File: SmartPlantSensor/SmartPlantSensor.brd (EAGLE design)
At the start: 25 x 100 mm, 13 parts

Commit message: Release v1.0.0
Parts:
- removed C5: 10nF, rcl:C0603
- removed U$1: TLC555CDR, HeRo:SOIC127P600X175-8
- removed U$2: ESP-12E, HeRo:ESP-12E
- added C1: 10nF, rcl:C0603
- added DS18B20: DS18B20Z+, MaximIntegrated:SOIC8
- added ESP-12E: ESP-12E, ESP:ESP-12E
- added JP10, JP11, JP12, JP13, JP14, JP3, JP4, JP5, JP6, JP7, JP8, JP9: (no value), pinhead:1X01
- added R10, R11, R7, R8, R9: 10k, rcl:R0603
- added TLC555: TLC555CD, TexasInstruments:SOIC8
- moved R6 1.53 mm to (7.24, 85.0), turned to 90 degrees
- moved R4 0.65 mm to (15.9, 92.8)
- moved C4 0.65 mm to (12.8, 92.8)
- moved R1 0.65 mm to (9.78, 85.5)
- moved C3 0.65 mm to (18.4, 88.3)
- moved R5 0.65 mm to (18.4, 91.3)
- moved C2 0.65 mm to (9.78, 89.5)
- moved R2 0.65 mm to (9.78, 87.5)
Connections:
- removed net N$7: C5.2, U$1.5
- new net 1WIRE: DS18B20.4, ESP-12E.19
- new net EN: ESP-12E.3, R7.1
- new net IO0: ESP-12E.18, JP6.1, R9.1
- new net IO12: ESP-12E.6, JP12.1
- new net IO13: ESP-12E.7, JP11.1
- new net IO14: ESP-12E.5, JP13.1
- new net IO15: ESP-12E.16, R8.2
- new net IO16: ESP-12E.4, JP14.1
- new net IO2: ESP-12E.17, R11.1
- new net N$1: C1.2, TLC555.5
- new net RST: ESP-12E.1, JP5.1, R10.1
- new net RXD: ESP-12E.21, JP8.1
- new net TXD: ESP-12E.22, JP7.1
- net +3V3: now also DS18B20.3, ESP-12E.8, JP3.1, JP9.1, R10.2, R11.2, R7.2, R9.2, TLC555.4, TLC555.8; no longer U$1.4, U$1.8, U$2.VCC
- net ADC: now also ESP-12E.2; no longer U$2.ADC
- net DISH: now also TLC555.7; no longer U$1.7
- net GND: now also C1.1, DS18B20.5, ESP-12E.15, JP10.1, JP4.1, R8.1, TLC555.1; no longer C5.1, U$1.1, U$2.GND
- net OUT: now also TLC555.3; no longer U$1.3
- net T: now also TLC555.2, TLC555.6; no longer U$1.2, U$1.6
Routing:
- net GND: track 1.63 -> 159.1 mm, vias 1 -> 3
- net SENSOR: track 10.0 -> 73.8 mm
- net RST: track 0.00 -> 28.4 mm, vias 0 -> 2
- net IO0: track 0.00 -> 15.8 mm, vias 0 -> 1
- net IO2: track 0.00 -> 11.6 mm, vias 0 -> 1
- net RXD: track 0.00 -> 10.8 mm, vias 0 -> 1
- net +3V3: track 7.56 -> 17.6 mm, vias 2 -> 4
- net TXD: track 0.00 -> 9.01 mm
- net 1WIRE: track 0.00 -> 7.14 mm, vias 0 -> 1
- net EN: track 0.00 -> 6.81 mm, vias 0 -> 1
- net IO15: track 0.00 -> 5.46 mm, vias 0 -> 1
- net IO16: track 0.00 -> 3.05 mm
- net IO14: track 0.00 -> 2.83 mm
- net IO12: track 0.00 -> 2.60 mm
- net IO13: track 0.00 -> 2.54 mm
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- added copper zone on layer 1, net GND
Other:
- outline, holes or cut-outs redrawn
- board text added: "Smart Plant Sensor"
- board text added: "https://github.com/xXAM22Xx/SmartPlantSensor"

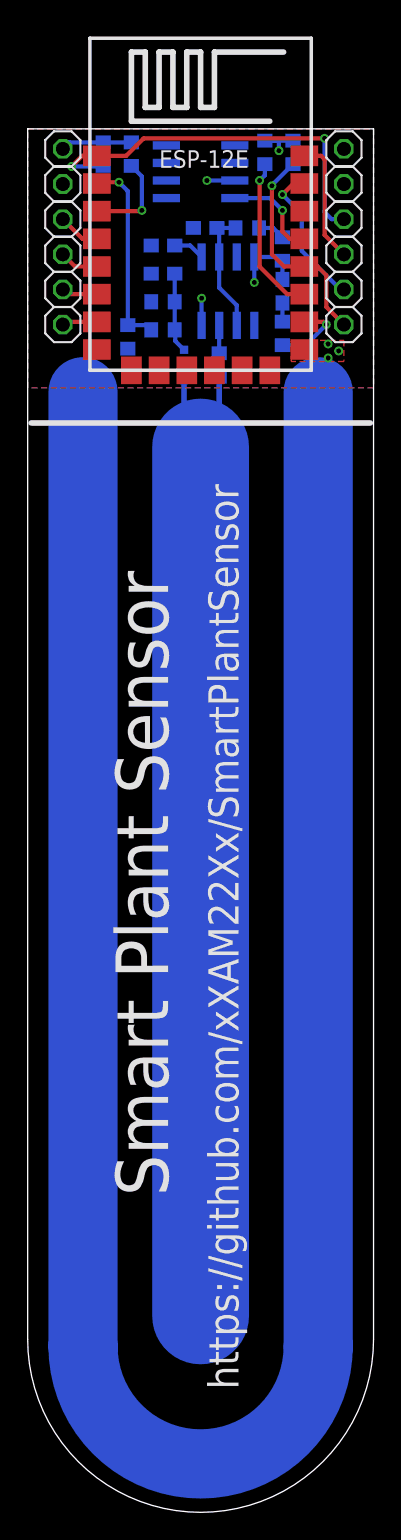
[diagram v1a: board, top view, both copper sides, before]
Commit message: Reworked Layout, added Protection
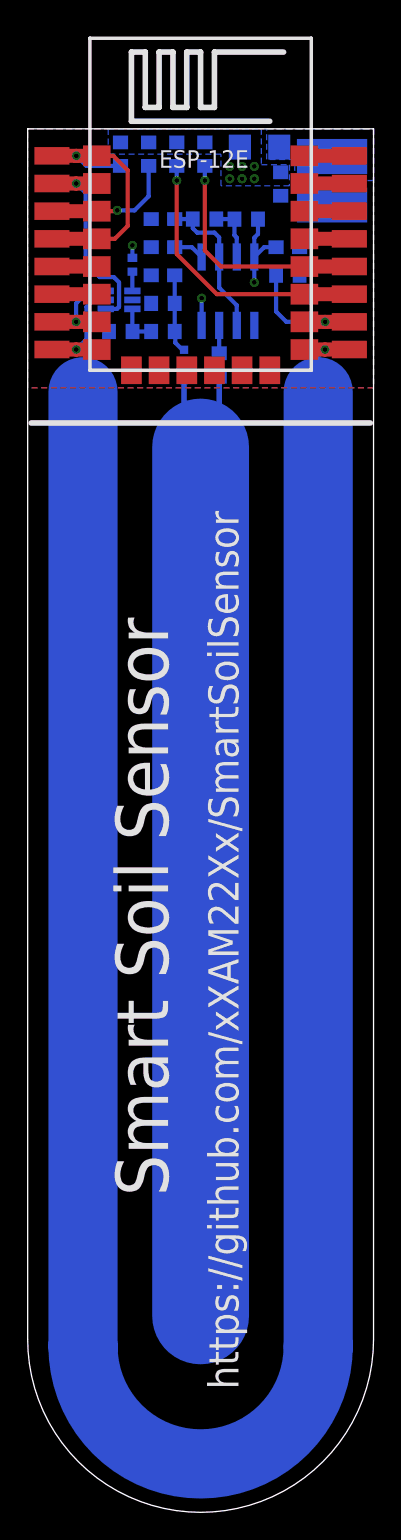
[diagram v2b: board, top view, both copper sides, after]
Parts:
- removed DS18B20: DS18B20Z+, MaximIntegrated:SOIC8
- removed JP10, JP11, JP12, JP13, JP14, JP3, JP4, JP5, JP6, JP7, JP8, JP9: (no value), pinhead:1X01
- added F1: FUSE, rcl:R1206
- added PAD1, PAD3: WIREPADSMD5-2,5, wirepad:5-2,5
- added PAD10, PAD11, PAD12, PAD13, PAD14, PAD15, PAD16, PAD17, PAD18, PAD19, PAD20, PAD5, PAD6, PAD7, PAD8, PAD9: (no value), wirepad:SMD1,27-2,54
- added R12: 0, rcl:R0402
- added U$1: TVS_BI_DIODE, HeRo:R0603
- added U$2: PI5A3157, HeRo:SOT65P210X110-6
- moved R11 6.37 mm to (10.8, 98.2)
- moved R9 6.37 mm to (12.8, 98.2)
- moved R8 4.23 mm to (18.8, 89.4), turned to 0 degrees
- moved R5 3.40 mm to (15.8, 93.5), turned to 0 degrees
- moved C3 3.20 mm to (18.8, 91.4), turned to 0 degrees
- moved R4 3.16 mm to (12.8, 93.5)
- moved C4 3.11 mm to (9.78, 93.5)
- moved R10 1.25 mm to (6.71, 98.2)
- moved R7 1.25 mm to (8.74, 98.2)
- moved R6 0.64 mm to (6.73, 85.4), turned to 180 degrees
- moved R1 0.12 mm to (9.78, 85.4)
- moved R2 0.12 mm to (9.78, 87.4)
- moved C1 0.12 mm to (9.78, 91.4)
- moved C2 0.12 mm to (9.78, 89.4)
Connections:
- removed net 1WIRE: DS18B20.4, ESP-12E.19
- removed net DISH: TLC555.7
- removed net IO16: ESP-12E.4, JP14.1
- new net IO4: ESP-12E.19, PAD16.1
- new net IO5: ESP-12E.20, PAD15.1
- new net N$4: R12.1, U$2.1
- new net SADC: R1.1, R6.2, U$2.3
- new net VCC: F1.1, PAD1.1
- net +3V3: now also F1.2, PAD12.1, R12.2, U$1.2, U$2.5; no longer DS18B20.3, JP3.1, JP9.1
- net ADC: now also PAD6.1, U$2.4; no longer R1.1, R6.2
- net DISCH: now also TLC555.7
- net EN: now also PAD7.1
- net GND: now also PAD20.1, PAD3.1, U$1.1, U$2.2; no longer DS18B20.5, JP10.1, JP4.1
- net IO0: now also PAD17.1; no longer JP6.1
- net IO12: now also PAD10.1; no longer JP12.1
- net IO13: now also PAD11.1, U$2.6; no longer JP11.1
- net IO14: now also PAD9.1; no longer JP13.1
- net IO15: now also PAD19.1
- net IO2: now also PAD18.1
- net RST: now also ESP-12E.4, PAD5.1, PAD8.1; no longer JP5.1
- net RXD: now also PAD14.1; no longer JP8.1
- net TXD: now also PAD13.1; no longer JP7.1
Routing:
- net RST: track 28.4 -> 19.3 mm, vias 2 -> 1
- net IO2: track 11.6 -> 20.0 mm
- net RXD: track 10.8 -> 3.25 mm, vias 1 -> 0
- net 1WIRE: track 7.14 -> 0.00 mm, vias 1 -> 0
- net TXD: track 9.01 -> 3.25 mm
- net IO13: track 2.54 -> 7.10 mm, vias 0 -> 1
- net IO15: track 5.46 -> 9.73 mm
- net IO5: track 0.00 -> 3.25 mm
- net IO4: track 0.00 -> 3.25 mm
- net IO16: track 3.05 -> 0.00 mm
- net SADC: track 0.00 -> 2.99 mm
- net EN: track 6.81 -> 9.64 mm
- net GND: track 159.1 -> 161.5 mm, vias 3 -> 1
- net DISCH: track 1.97 -> 4.12 mm
- net T: track 8.99 -> 11.0 mm
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- added copper zone on layer 16, net +3V3
- added copper zone on layer 16, net VCC
- removed copper zone on layer 1, net GND
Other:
- board text added: "Smart Soil Sensor"
- board text added: "https://github.com/xXAM22Xx/SmartSoilSensor"
- board text removed: "Smart Plant Sensor"
- board text removed: "https://github.com/xXAM22Xx/SmartPlantSensor"
